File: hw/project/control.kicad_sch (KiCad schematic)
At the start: 49 parts, among them SW1 RESET, SW2 BOOT0, U7 STSPIN32G4, X1 32MHZ 10PF

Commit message: Done control :)
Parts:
- removed R1: 0, Resistor_SMD:R_0603_1608Metric, symbol Device:R_Small_US
- added R84: 0, Resistor_SMD:R_0603_1608Metric, symbol Device:R_Small_US
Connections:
- net OSC_OUT: now also R84.2
- net at C2.1, X1.3: now also R84.1
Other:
- note added: "*Route both at EPAD: 1. Gate Drivers Power Ground (PGND) -> Zone near VM_IN connector and low-side MOSFETs 2. Control Logic Ground (VSS) -> Zone near MCU application circuitry"
- note added: "verify in STM32CubeIDE before starting layout"
- moved on the sheet: C1, C2, C4, C8, D29, R12, R8, R82, R83, TH1, TP16, TP17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

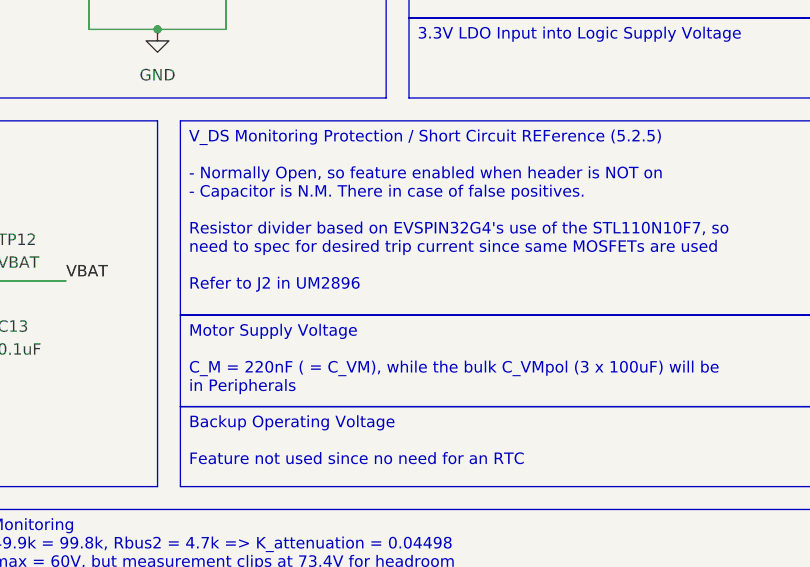
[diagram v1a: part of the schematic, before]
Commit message: Finalize phase voltage sensing
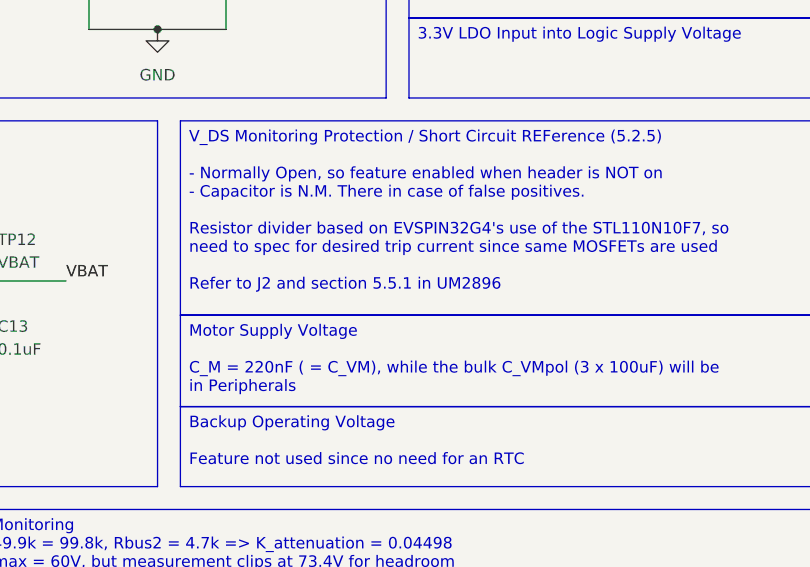
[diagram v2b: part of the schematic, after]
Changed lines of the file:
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@@
 		)
 	)
-	(text_box "V_DS Monitoring Protection / Short Circuit REFerence (5.2.5)\n\n- Normally Open, so feature enabled when header is NOT on\n- Capacitor is N.M. There in case of false positives.\n\nResistor divider based on EVSPIN32G4's use of the STL110N10F7, so need to spec for desired trip current since same MOSFETs are used\n\nRefer to J2 in UM2896"
+	(text_box "V_DS Monitoring Protection / Short Circuit REFerence (5.2.5)\n\n- Normally Open, so feature enabled when header is NOT on\n- Capacitor is N.M. There in case of false positives.\n\nResistor divider based on EVSPIN32G4's use of the STL110N10F7, so need to spec for desired trip current since same MOSFETs are used\n\nRefer to J2 and section 5.5.1 in UM2896"
 		(exclude_from_sim no)
 		(at 210.82 91.44 0)

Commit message: Finalize drive sheet
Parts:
- added R94: 0, Resistor_SMD:R_0603_1608Metric, symbol Device:R_Small_US
- D1: value 100V -> STPS1H100A
- D29: value BAT30K -> BAT30KFILM
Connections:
- net GND: now also R94.1; no longer U7.32 (PGND)
- new net PGND: R94.2, U7.32 (PGND)
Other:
- moved on the sheet: C11, C15, C17, C6, C7, D1, L1, R11, TP11, TP13, TP14, TP17

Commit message: Change relevant GND symbols to PGND
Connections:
- net GND: no longer C6.1, C7.1, C9.1, D1.2
- net PGND: now also C6.1, C7.1, C9.1, D1.2
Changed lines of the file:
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@@
 	)
 	(symbol
-		(lib_id "power:GND")
-		(at 121.92 81.28 0)
-		(unit 1)
-		(body_style 1)
-		(exclude_from_sim no)
-		(in_bom yes)
-		(on_board yes)
-		(in_pos_files yes)
-		(dnp no)
-		(fields_autoplaced yes)
-		(property "Reference" "#PWR018"
-			(at 121.92 87.63 0)
-			(hide yes)
-			(show_name no)
-			(do_not_autoplace no)
-			(effects
-				(font
-					(size 1.27 1.27)
-				)
-			)
-		)
-		(property "Value" "GND"
-			(at 121.92 86.36 0)
-			(show_name no)
-			(do_not_autoplace no)
-			(effects
-				(font
-					(size 1.27 1.27)
-				)
-			)
-		)
-		(property "Footprint" ""
-			(at 121.92 81.28 0)
-			(hide yes)
-			(show_name no)
-			(do_not_autoplace no)
-			(effects
-				(font
-					(size 1.27 1.27)
-				)
-			)
-		)
-		(property "Datasheet" ""
-			(at 121.92 81.28 0)
-			(hide yes)
-			(show_name no)
-			(do_not_autoplace no)
-			(effects
-				(font
-					(size 1.27 1.27)
-				)
-			)
-		)
-		(property "Description" "Power symbol creates a global label with name \"GND\" , ground"
-			(at 121.92 81.28 0)
-			(hide yes)
-			(show_name no)
-			(do_not_autoplace no)
-			(effects
-				(font
-					(size 1.27 1.27)
-				)
-			)
-		)
-		(pin "1"
-		)
-		(instances
-			(project "esc"
-				(path "/86a17c4d-db96-42a1-af84-d43fe593f4e6/50f7e8ea-49d2-4d3d-890c-dc3d94742dd9"
-					(reference "#PWR018")
-					(unit 1)
-				)
-			)
-		)
-	)
-	(symbol
 		(lib_id "esc:STSPIN32G4")
 		(at 33.02 27.94 0)
@@
 	(symbol
 		(lib_id "power:GND")
+		(at 154.94 121.92 0)
+		(unit 1)
+		(body_style 1)
+		(exclude_from_sim no)
+		(in_bom yes)
+		(on_board yes)
+		(in_pos_files yes)
+		(dnp no)
+		(fields_autoplaced yes)
+		(property "Reference" "#PWR076"
+			(at 154.94 128.27 0)
+			(hide yes)
+			(show_name no)
+			(do_not_autoplace no)
+			(effects
+				(font
+					(size 1.27 1.27)
+				)
+			)
+		)
+		(property "Value" "PGND"
+			(at 154.94 127 0)
+			(show_name no)
+			(do_not_autoplace no)
+			(effects
+				(font
+					(size 1.27 1.27)
+				)
+			)
+		)
+		(property "Footprint" ""
+			(at 154.94 121.92 0)
+			(hide yes)
+			(show_name no)
+			(do_not_autoplace no)
+			(effects
+				(font
+					(size 1.27 1.27)
+				)
+			)
+		)
+		(property "Datasheet" ""
+			(at 154.94 121.92 0)
+			(hide yes)
+			(show_name no)
+			(do_not_autoplace no)
+			(effects
+				(font
+					(size 1.27 1.27)
+				)
+			)
+		)
+		(property "Description" "Power symbol creates a global label with name \"GND\" , ground"
+			(at 154.94 121.92 0)
+			(hide yes)
+			(show_name no)
+			(do_not_autoplace no)
+			(effects
+				(font
+					(size 1.27 1.27)
+				)
+			)
+		)
+		(pin "1"
+		)
+		(instances
+			(project "esc"
+				(path "/86a17c4d-db96-42a1-af84-d43fe593f4e6/50f7e8ea-49d2-4d3d-890c-dc3d94742dd9"
+					(reference "#PWR076")
+					(unit 1)
+				)
+			)
+		)
+	)
+	(symbol
+		(lib_id "power:GND")
 		(at 210.82 81.28 0)
 		(unit 1)
@@
 	)
 	(symbol
+		(lib_id "power:GND")
+		(at 121.92 81.28 0)
+		(unit 1)
+		(body_style 1)
+		(exclude_from_sim no)
+		(in_bom yes)
+		(on_board yes)
+		(in_pos_files yes)
+		(dnp no)
+		(fields_autoplaced yes)
+		(property "Reference" "#PWR070"
+			(at 121.92 87.63 0)
+			(hide yes)
+			(show_name no)
+			(do_not_autoplace no)
+			(effects
+				(font
+					(size 1.27 1.27)
+				)
+			)
+		)
+		(property "Value" "PGND"
+			(at 121.92 86.36 0)
+			(show_name no)
+			(do_not_autoplace no)
+			(effects
+				(font
+					(size 1.27 1.27)
+				)
+			)
+		)
+		(property "Footprint" ""
+			(at 121.92 81.28 0)
+			(hide yes)
+			(show_name no)
+			(do_not_autoplace no)
+			(effects
+				(font
+					(size 1.27 1.27)
+				)
+			)
+		)
+		(property "Datasheet" ""
+			(at 121.92 81.28 0)
+			(hide yes)
+			(show_name no)
+			(do_not_autoplace no)
+			(effects
+				(font
+					(size 1.27 1.27)
+				)
+			)
+		)
+		(property "Description" "Power symbol creates a global label with name \"GND\" , ground"
+			(at 121.92 81.28 0)
+			(hide yes)
+			(show_name no)
+			(do_not_autoplace no)
+			(effects
+				(font
+					(size 1.27 1.27)
+				)
+			)
+		)
+		(pin "1"
+		)
+		(instances
+			(project "esc"
+				(path "/86a17c4d-db96-42a1-af84-d43fe593f4e6/50f7e8ea-49d2-4d3d-890c-dc3d94742dd9"
+					(reference "#PWR070")
+					(unit 1)
+				)
+			)
+		)
+	)
+	(symbol
 		(lib_id "Device:R_Small_US")
 		(at 96.52 156.21 0)
@@
 					(unit 1)
 				)
-			)
-		)
-	)
-	(symbol
-		(lib_id "power:GND")
-		(at 154.94 121.92 0)
-		(unit 1)
-		(body_style 1)
-		(exclude_from_sim no)
-		(in_bom yes)
-		(on_board yes)
-		(in_pos_files yes)
-		(dnp no)
-		(fields_autoplaced yes)
-		(property "Reference" "#PWR023"
-			(at 154.94 128.27 0)
-			(hide yes)
-			(show_name no)
-			(do_not_autoplace no)
-			(effects
-				(font
-					(size 1.27 1.27)
-				)
-			)
-		)
-		(property "Value" "GND"
-			(at 154.94 127 0)
-			(show_name no)
-			(do_not_autoplace no)
-			(effects
-				(font
-					(size 1.27 1.27)
-				)
-			)
-		)
-		(property "Footprint" ""
-			(at 154.94 121.92 0)
-			(hide yes)
-			(show_name no)
-			(do_not_autoplace no)
-			(effects
-				(font
-					(size 1.27 1.27)
-				)
-			)
-		)
-		(property "Datasheet" ""
-			(at 154.94 121.92 0)
-			(hide yes)
-			(show_name no)
-			(do_not_autoplace no)
-			(effects
-				(font
-					(size 1.27 1.27)
-				)
-			)
-		)
-		(property "Description" "Power symbol creates a global label with name \"GND\" , ground"
-			(at 154.94 121.92 0)
-			(hide yes)
-			(show_name no)
-			(do_not_autoplace no)
-			(effects
-				(font
-					(size 1.27 1.27)
-				)
-			)
-		)
-		(pin "1"
-		)
-		(instances
-			(project "esc"
-				(path "/86a17c4d-db96-42a1-af84-d43fe593f4e6/50f7e8ea-49d2-4d3d-890c-dc3d94742dd9"
-					(reference "#PWR023")
-					(unit 1)
-				)

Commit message: Prep to revamp power sheet
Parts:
- added TP18: GND, KEYSTONE_5016:KEYSTONE_5016, symbol Connector:TestPoint
- added TP19: PGND, KEYSTONE_5016:KEYSTONE_5016, symbol Connector:TestPoint
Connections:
- net GND: now also TP18.1
- net PGND: now also TP19.1
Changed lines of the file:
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@@
 	)
 	(junction
+		(at 154.94 120.65)
+		(diameter 0)
+		(color 0 0 0 0)
+	)
+	(junction
 		(at 153.67 172.72)
 		(diameter 0)
@@
 	)
 	(junction
+		(at 203.2 81.28)
+		(diameter 0)
+		(color 0 0 0 0)
+	)
+	(junction
 		(at 137.16 68.58)
 		(diameter 0)
@@
 	(wire
 		(pts
-			(xy 154.94 118.11) (xy 154.94 121.92)
+			(xy 200.66 81.28) (xy 203.2 81.28)
+		)
+		(stroke
+			(width 0)
+			(type default)
+		)
+	)
+	(wire
+		(pts
+			(xy 154.94 118.11) (xy 154.94 120.65)
+		)
+		(stroke
+			(width 0)
+			(type default)
+		)
+	)
+	(wire
+		(pts
+			(xy 154.94 120.65) (xy 154.94 121.92)
 		)
 		(stroke
@@
 	(wire
 		(pts
+			(xy 152.4 120.65) (xy 154.94 120.65)
+		)
+		(stroke
+			(width 0)
+			(type default)
+		)
+	)
+	(wire
+		(pts
 			(xy 203.2 66.04) (xy 203.2 68.58)
 		)
@@
 	)
 	(symbol
+		(lib_id "Connector:TestPoint")
+		(at 200.66 81.28 90)
+		(unit 1)
+		(body_style 1)
+		(exclude_from_sim no)
+		(in_bom yes)
+		(on_board yes)
+		(in_pos_files yes)
+		(dnp no)
+		(fields_autoplaced yes)
+		(property "Reference" "TP18"
+			(at 197.358 76.2 90)
+			(show_name no)
+			(do_not_autoplace no)
+			(effects
+				(font
+					(size 1.27 1.27)
+				)
+			)
+		)
+		(property "Value" "GND"
+			(at 197.358 78.74 90)
+			(show_name no)
+			(do_not_autoplace no)
+			(effects
+				(font
+					(size 1.27 1.27)
+				)
+			)
+		)
+		(property "Footprint" "KEYSTONE_5016:KEYSTONE_5016"
+			(at 200.66 76.2 0)
+			(hide yes)
+			(show_name no)
+			(do_not_autoplace no)
+			(effects
+				(font
+					(size 1.27 1.27)
+				)
+			)
+		)
+		(property "Datasheet" "https://www.digikey.ca/en/products/detail/keystone-electronics/5016/278887"
+			(at 200.66 76.2 0)
+			(hide yes)
+			(show_name no)
+			(do_not_autoplace no)
+			(effects
+				(font
+					(size 1.27 1.27)
+				)
+			)
+		)
+		(property "Description" "test point"
+			(at 200.66 81.28 0)
+			(hide yes)
+			(show_name no)
+			(do_not_autoplace no)
+			(effects
+				(font
+					(size 1.27 1.27)
+				)
+			)
+		)
+		(pin "1"
+		)
+		(instances
+			(project "esc"
+				(path "/86a17c4d-db96-42a1-af84-d43fe593f4e6/50f7e8ea-49d2-4d3d-890c-dc3d94742dd9"
+					(reference "TP18")
+					(unit 1)
+				)
+			)
+		)
+	)
+	(symbol
 		(lib_id "power:VDD")
 		(at 177.8 25.4 0)
@@
 					(unit 1)
 				)
+			)
+		)
+	)
+	(symbol
+		(lib_id "Connector:TestPoint")
+		(at 152.4 120.65 90)
+		(unit 1)
+		(body_style 1)
+		(exclude_from_sim no)
+		(in_bom yes)
+		(on_board yes)
+		(in_pos_files yes)
+		(dnp no)
+		(fields_autoplaced yes)
+		(property "Reference" "TP19"
+			(at 149.098 115.57 90)
+			(show_name no)
+			(do_not_autoplace no)
+			(effects
+				(font
+					(size 1.27 1.27)
+				)
+			)
+		)
+		(property "Value" "PGND"
+			(at 149.098 118.11 90)
+			(show_name no)
+			(do_not_autoplace no)
+			(effects
+				(font
+					(size 1.27 1.27)
+				)
+			)
+		)
+		(property "Footprint" "KEYSTONE_5016:KEYSTONE_5016"
+			(at 152.4 115.57 0)
+			(hide yes)
+			(show_name no)
+			(do_not_autoplace no)
+			(effects
+				(font
+					(size 1.27 1.27)
+				)
+			)
+		)
+		(property "Datasheet" "https://www.digikey.ca/en/products/detail/keystone-electronics/5016/278887"
+			(at 152.4 115.57 0)
+			(hide yes)
+			(show_name no)
+			(do_not_autoplace no)
+			(effects
+				(font
+					(size 1.27 1.27)
+				)
+			)
+		)
+		(property "Description" "test point"
+			(at 152.4 120.65 0)
+			(hide yes)
+			(show_name no)
+			(do_not_autoplace no)
+			(effects
+				(font
+					(size 1.27 1.27)
+				)
+			)
+		)
+		(pin "1"
+		)
+		(instances
+			(project "esc"
+				(path "/86a17c4d-db96-42a1-af84-d43fe593f4e6/50f7e8ea-49d2-4d3d-890c-dc3d94742dd9"
+					(reference "TP19")
+					(unit 1)
+				)

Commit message: Continuing power revamp tomorrow
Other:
- note added: "tying resistor still same after power sheet revamp?"
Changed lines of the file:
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@@
+		)
+	)
+	(text "tying resistor still same after power sheet revamp?"
+		(exclude_from_sim no)
+		(at 70.358 162.306 0)
+		(effects
+			(font
+				(size 1.27 1.27)
+				(color 255 4 4 1)
+			)
+			(justify right)
 		)
 	)

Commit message: Checkpoint: Ready to spec rest of power stage tom
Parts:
- removed R81: 0, Resistor_SMD:R_0603_1608Metric, symbol Device:R_Small_US
- added FB1: 600@100MHz, Inductor_SMD:L_0201_0603Metric, symbol Device:FerriteBead_Small
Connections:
- net VDD: now also FB1.2; no longer C10.1
- net VDDA: now also C10.1, FB1.1; no longer C14.1
- net VREF+: now also C14.1
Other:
- moved on the sheet: R14, TP1

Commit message: Spec LEDs
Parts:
- removed C4, C8: 33nF, Capacitor_SMD:C_0603_1608Metric, symbol Device:C_Small
- removed R5: 22k, Resistor_SMD:R_0603_1608Metric, symbol Device:R_Small_US
- removed R82, R83: 49.9k/1%, Resistor_SMD:R_0603_1608Metric, symbol Device:R_Small_US
- added C20, C28: 0.1uF, Capacitor_SMD:C_0603_1608Metric, symbol Device:C_Small
- added R109: 10k, Resistor_SMD:R_0603_1608Metric, symbol Device:R_Small_US
- added R31: 22.1k, Resistor_SMD:R_0603_1608Metric, symbol Device:R_Small_US
- added R44: 118k, Resistor_SMD:R_0603_1608Metric, symbol Device:R_Small_US
- R12: value 4.7k/1% -> 4.7k/0.1W
- U7: footprint esc:QFN_IN32G4_STM -> STSPIN32G4:QFN_IN32G4_STM
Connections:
- net BOOT0: now also R109.2; no longer R9.1, SW2.1
- net GND: now also C20.1, C28.1
- net PCB_TEMP: now also C28.2
- net SCREF: now also R31.2
- net VDD: now also R31.1
- net VM: now also R44.1
- net VM_SENSE: now also C20.2, R44.2
- new net: R109.1, R9.1, SW2.1
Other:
- moved on the sheet: SW2
